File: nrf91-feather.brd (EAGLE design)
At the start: 50.8 x 22.9 mm, 81 parts, among them J1 CON-USB-1050170001, J2 CON-HEADER-1X12-MALE-PIN, J3 CON-HEADER-1X16-MALE-PIN, J4 1909763-1, J5 104224-0820, J6 CON-S2B-PH-SM4-TB(LF)(SN), J7 1909763-1, J9 CON-0002, Q1 MOSFET-P-SC89, Q2 MOSFET-DUAL-COMP-VMT6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

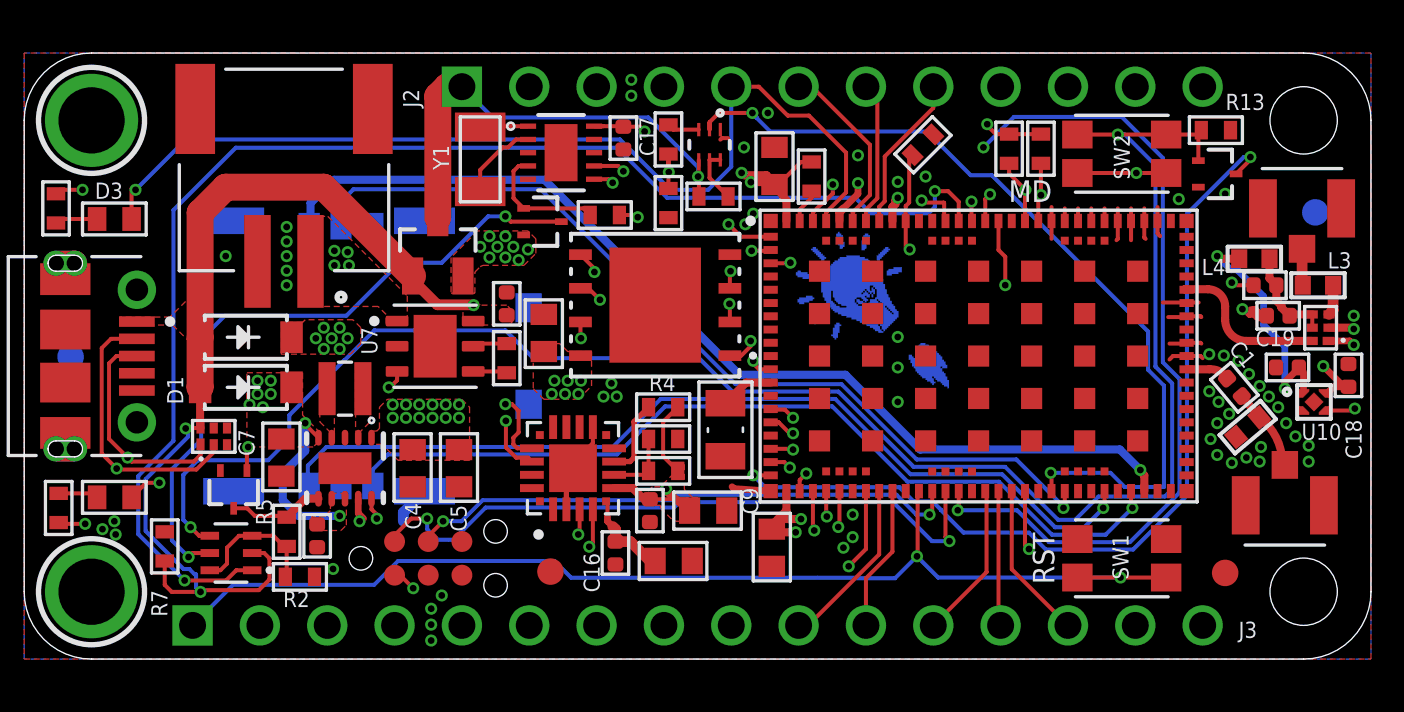
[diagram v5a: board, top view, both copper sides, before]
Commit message: 1. Changing name of design to nRF9160 Feather 2. Fixing holes with BOM export.
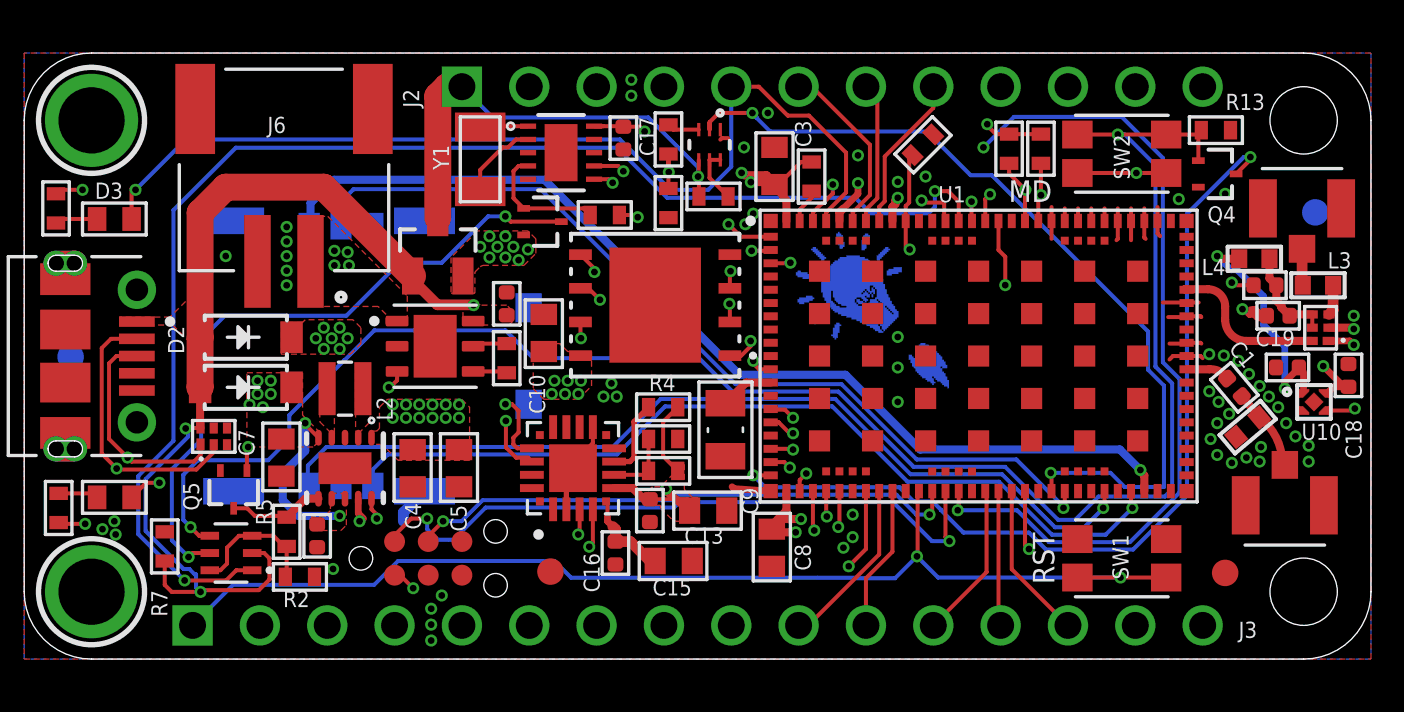
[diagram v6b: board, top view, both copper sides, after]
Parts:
- added SOLDER1: SOLDER-PASTE-ROOM-TEMP-50G, wolff-den:PLACEHOLDER
- PCB1: value PCB-SARA-R410-02B -> PCB-NRF91-FEATHER
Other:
- board text added: "nRF9160 Feather"
- board text removed: "nRF91 Featherwing"

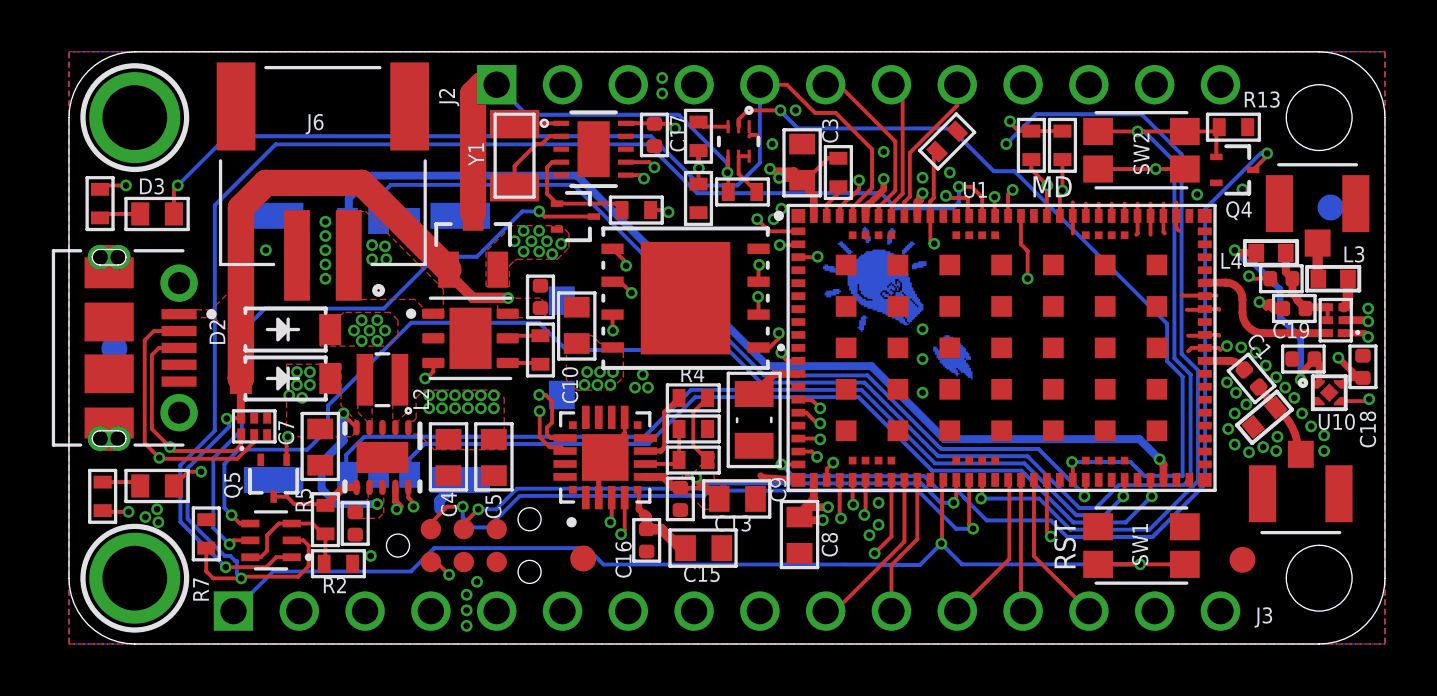
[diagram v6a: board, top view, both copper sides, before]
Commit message: 1. Adding pulldown on EN pin
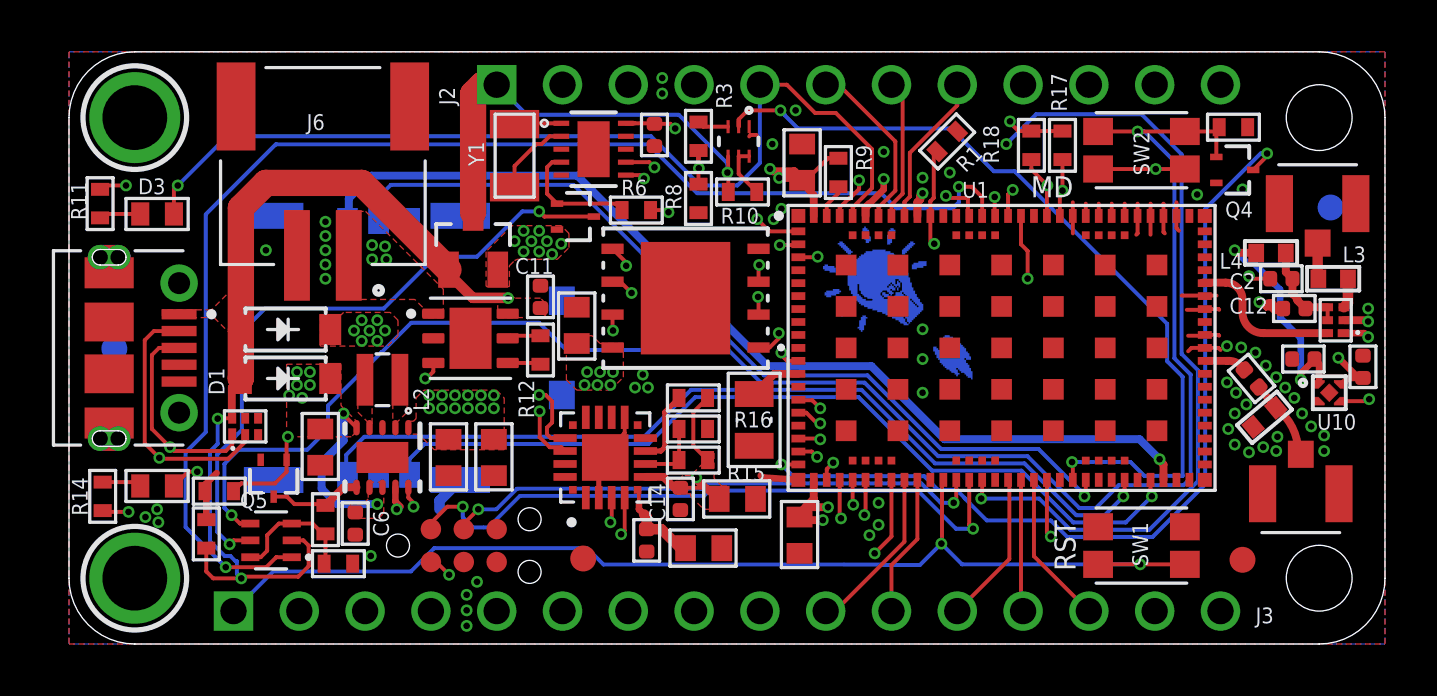
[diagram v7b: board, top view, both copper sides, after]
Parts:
- added R19: 1M, wolff-den:R0402-M
- moved SOLDER1 290.9 mm to (19.3, 33.4)
- moved U5 0.35 mm to (6.80, 8.40)
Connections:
- net !EN: now also R19.2
- net GND: now also R19.1
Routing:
- net !EN: track 19.8 -> 22.6 mm
- net GND: track 34.6 -> 36.6 mm
- net VBUS: track 55.9 -> 55.1 mm

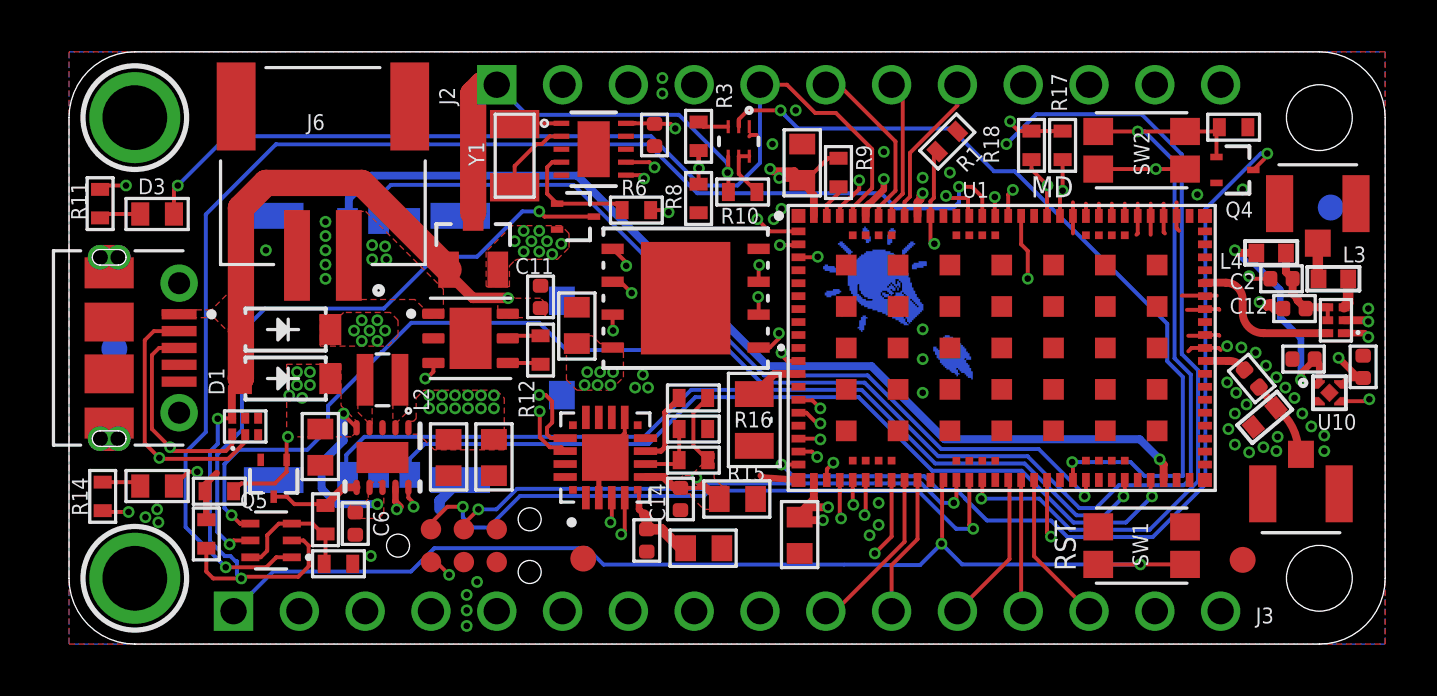
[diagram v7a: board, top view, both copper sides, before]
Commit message: Circuitry for external active GPS antenna.
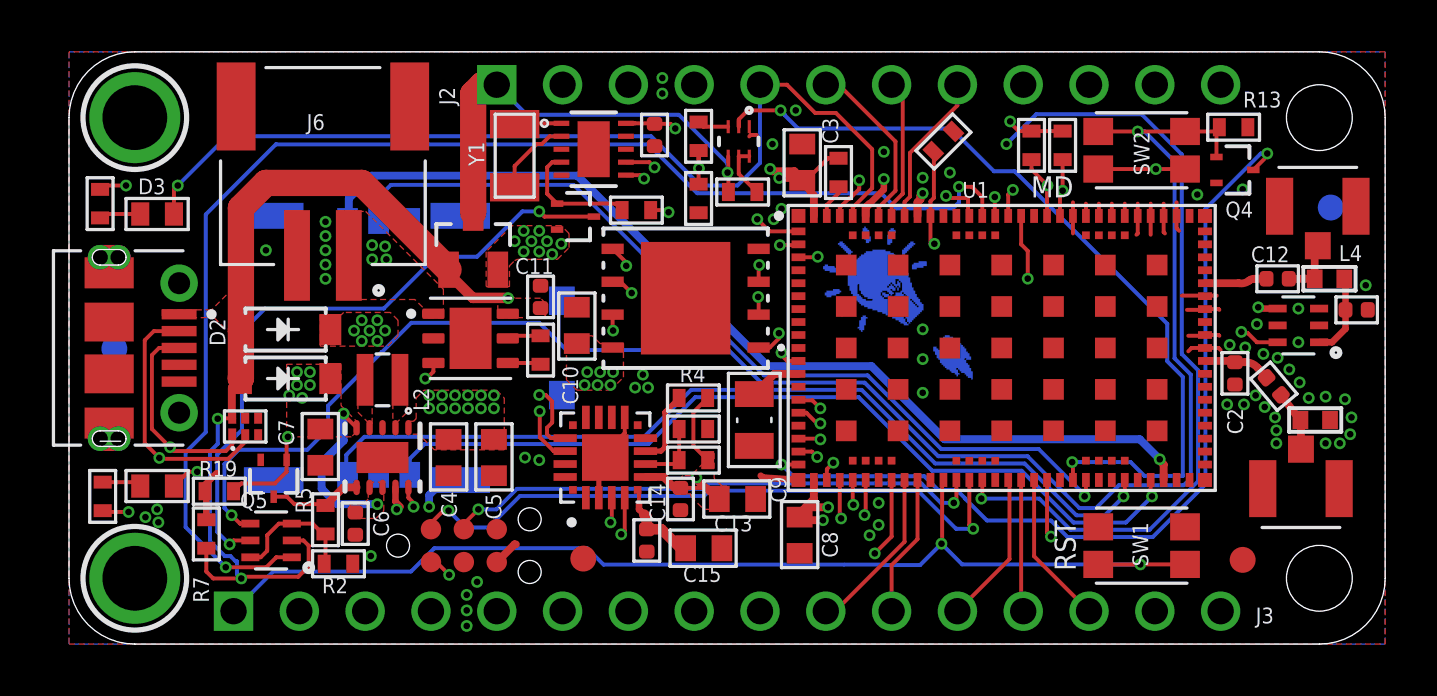
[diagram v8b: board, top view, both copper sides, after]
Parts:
- removed C18: 1u, wolff-den:CAPC1005X55N
- removed L3: 5.6n, wolff-den:IND0402_22N_TAI
- removed U10: (no value), wolff-den:DFN4
- C12: value 100p -> 56p
- C19: value 1u -> 56p
- C2: value 0.1u -> 15p
- L4: value 5.6n -> 68n
- U4: value BGU6005,115 -> POWER-SWITCH-MIC94092YC6; device wolff-den:PSON50P100X145X50-6N -> wolff-den:SOT363
- moved U$5 246.9 mm to (-176.2, -115.0), turned to 0 degrees
- moved C2 4.07 mm to (45.0, 10.4), turned to 270 degrees
- moved C19 2.80 mm to (49.7, 12.9), turned to 0 degrees
- moved L4 2.46 mm to (48.6, 14.1), turned to 180 degrees
- moved L1 1.95 mm to (48.1, 8.65), turned to 180 degrees
- moved U4 1.46 mm to (47.5, 12.3), turned to 90 degrees
- moved C12 1.32 mm to (46.6, 14.1), turned to 0 degrees
- moved C1 0.90 mm to (46.5, 9.95)
- moved J4 0.20 mm to (47.5, 6.00)
- moved R1 0.15 mm to (33.8, 19.4)
- moved J7 0.10 mm to (48.2, 16.9)
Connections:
- removed net GPS_AMP: L3.2, U4.3
- removed net GPS_CON: J7.1, L3.1
- removed net VCC_1V8: C19.1, L4.1, U10.1
- removed net VCC_LNA_FILT: C12.1, C2.1, L4.2, U4.4, U4.5
- new net GPS_ANT: C12.2, J7.1, L4.2
- new net LNA_SW_OUT: C19.1, L4.1, U4.1
- net +3V3: now also U4.4; no longer C18.1, U10.4
- net ANT: now also C2.1
- net GND: now also U4.5; no longer C12.2, C18.2, U10.2, U4.1
- net GPS: now also C12.1; no longer U4.6
- net LNA_EN: now also U4.6; no longer U10.3
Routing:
- net VCC_1V8: track 9.17 -> 0.00 mm, vias 2 -> 0
- net LNA_EN: track 25.2 -> 18.8 mm
- net VCC_LNA_FILT: track 3.84 -> 0.00 mm
- net GND: track 36.6 -> 32.9 mm, vias 64 -> 65
- net GPS: track 5.99 -> 2.40 mm
- net LNA_SW_OUT: track 0.00 -> 3.22 mm
- net GPS_ANT: track 0.00 -> 2.32 mm
- net GPS_CON: track 1.39 -> 0.00 mm
- net +3V3: track 18.4 -> 17.2 mm
- net GPS_AMP: track 1.16 -> 0.00 mm
- net ANT: track 1.62 -> 2.62 mm
- net ANT_FILT: track 3.09 -> 2.38 mm
